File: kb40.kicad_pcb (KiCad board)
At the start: 2 copper layers, 4.8 x 4.8 mm, 73 parts, among them SW1 Choc, SW10 Choc, SW11 Choc, SW12 Choc, SW13 Choc, SW14 Choc, SW15 Choc, SW16 Choc, SW17 Choc, SW18 Choc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

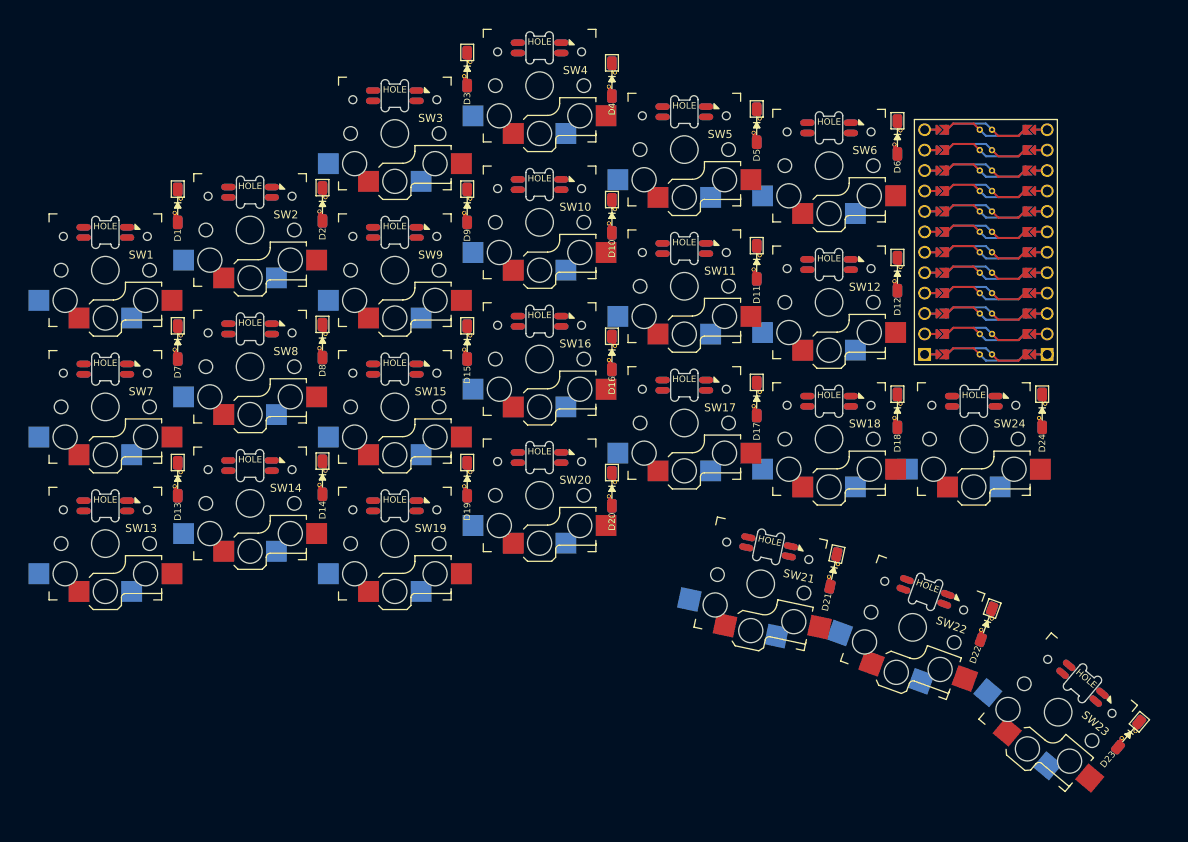
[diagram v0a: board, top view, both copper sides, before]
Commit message: generate test step file
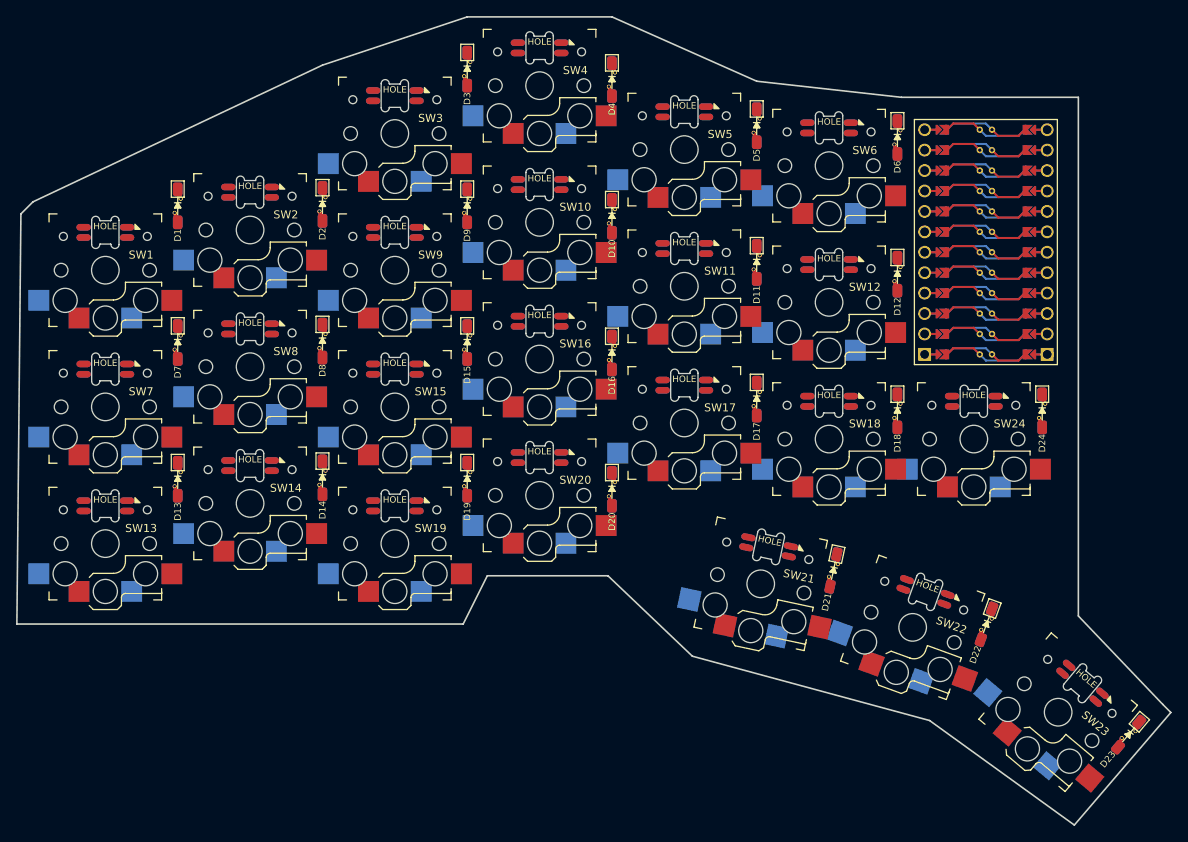
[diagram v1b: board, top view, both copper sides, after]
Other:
- board size 4.8 x 4.8 mm -> 143.5 x 100.5 mm
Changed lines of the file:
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@@
       (net 60 "COL5") (pinfunction "2") (pintype "passive"))
   )
+  (gr_poly
+    (pts
+      (xy 154.5 53)
+      (xy 172.5 55)
+      (xy 194.5 55)
+      (xy 194.5 119.5)
+      (xy 205 130.5)
+      (xy 206 131.5)
+      (xy 194 145.5)
+      (xy 176 132.5)
+      (xy 146.5 124.5)
+      (xy 136 114.5)
+      (xy 121 114.5)
+      (xy 118 120.5)
+      (xy 62.5 120.5)
+      (xy 63 69.5)
+      (xy 64.5 68)
+      (xy 100.5 51)
+      (xy 118.5 45)
+      (xy 136.5 45)
+    ) (layer "Edge.Cuts") (width 0.2) (fill none))
   (group "" (id 1eb147e1-589d-4513-90a6-3c68c18e557f)
     (members

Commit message: initial matrix routing
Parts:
- added J1: TRRS, pro-micro:PJ-320A, F.Cu at (190.5, 110.0)
- added J2: OLED, Connector_PinSocket_2.54mm:PinSocket_1x04_P2.54mm_Vertical, F.Cu at (186.8, 87.8)
- added JP1: SJ, Jumper:SolderJumper-2_P1.3mm_Open_TrianglePad1.0x1.5mm, F.Cu at (178.6, 84.2)
- added JP2: SJ, Jumper:SolderJumper-2_P1.3mm_Open_TrianglePad1.0x1.5mm, F.Cu at (181.4, 84.2)
- added JP3: SJ, Jumper:SolderJumper-2_P1.3mm_Open_TrianglePad1.0x1.5mm, F.Cu at (184.6, 84.2)
- added JP4: SJ, Jumper:SolderJumper-2_P1.3mm_Open_TrianglePad1.0x1.5mm, F.Cu at (187.4, 84.2)
- added JP5: SJ, Jumper:SolderJumper-2_P1.3mm_Open_TrianglePad1.0x1.5mm, B.Cu at (178.6, 84.2)
- added JP6: SJ, Jumper:SolderJumper-2_P1.3mm_Open_TrianglePad1.0x1.5mm, B.Cu at (181.4, 84.2)
- added JP7: SJ, Jumper:SolderJumper-2_P1.3mm_Open_TrianglePad1.0x1.5mm, B.Cu at (184.6, 84.2)
- added JP8: SJ, Jumper:SolderJumper-2_P1.3mm_Open_TrianglePad1.0x1.5mm, B.Cu at (187.4, 84.2)
- moved U1 6.00 mm to (183.0, 67.0), turned to -90 degrees
- moved D1 2.00 mm to (82.5, 70.5)
- moved D13 2.00 mm to (82.5, 104.5)
- moved D14 2.00 mm to (100.5, 104.3)
- moved D2 2.00 mm to (100.5, 70.3)
- moved D7 2.00 mm to (82.5, 87.5)
- moved D8 2.00 mm to (100.5, 87.3)
- moved LED1 2.00 mm to (73.5, 73.8)
- moved LED13 2.00 mm to (73.5, 107.8)
- moved LED14 2.00 mm to (91.5, 102.8)
- moved LED2 2.00 mm to (91.5, 68.8)
- moved LED7 2.00 mm to (73.5, 90.8)
- moved LED8 2.00 mm to (91.5, 85.8)
- moved SW1 2.00 mm to (73.5, 78.5)
- moved SW13 2.00 mm to (73.5, 112.5)
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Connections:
- U1 pad 23: unconnected-(U1-Pad23) -> GND
- U1 pad 3: unconnected-(U1-Pad3) -> GND
- U1 pad 4: unconnected-(U1-Pad4) -> GND
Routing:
- net COL2: track 0.00 -> 201.5 mm, vias 0 -> 6
- net COL3: track 0.00 -> 183.4 mm, vias 0 -> 6
- net COL4: track 0.00 -> 175.5 mm, vias 0 -> 6
- net ROW3: track 0.00 -> 168.8 mm, vias 0 -> 4
- net COL1: track 0.00 -> 166.2 mm, vias 0 -> 5
- net COL0: track 0.00 -> 161.8 mm, vias 0 -> 4
- net ROW1: track 0.00 -> 154.6 mm, vias 0 -> 5
- net ROW0: track 0.00 -> 154.4 mm
- net ROW2: track 0.00 -> 154.0 mm, vias 0 -> 5
- net COL5: track 0.00 -> 122.5 mm, vias 0 -> 4
- net Net-(D9-Pad2): track 0.00 -> 23.5 mm, vias 0 -> 1
- net Net-(D1-Pad2): track 0.00 -> 23.5 mm, vias 0 -> 1
- net Net-(D15-Pad2): track 0.00 -> 23.4 mm, vias 0 -> 1
- net Net-(D7-Pad2): track 0.00 -> 23.4 mm, vias 0 -> 1
- net Net-(D19-Pad2): track 0.00 -> 23.4 mm, vias 0 -> 1
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- added copper zone on B.Cu, net GND
- added copper zone on F.Cu, net GND
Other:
- board size 143.5 x 100.5 mm -> 144.3 x 102.7 mm

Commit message: initial rgb routing
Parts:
- LED1, LED10, LED11, LED12, LED13, LED14, LED15, LED16, LED17, LED18, LED19, LED2, LED20, LED21, LED22, LED23, LED24, LED3, LED4, LED5, LED6, LED7, LED8, LED9: footprint tufourn-components:SK6812Mini-E -> tufourn-components:SK6812-MINI-E
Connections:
- LED1 pad 4: VDD -> VCC
- LED10 pad 4: VDD -> VCC
- LED11 pad 4: VDD -> VCC
- LED12 pad 4: VDD -> VCC
- LED13 pad 4: VDD -> VCC
- LED14 pad 4: VDD -> VCC
- LED15 pad 4: VDD -> VCC
- LED16 pad 4: VDD -> VCC
- LED17 pad 4: VDD -> VCC
- LED18 pad 4: VDD -> VCC
- LED19 pad 4: VDD -> VCC
- LED2 pad 4: VDD -> VCC
- LED20 pad 4: VDD -> VCC
- LED21 pad 4: VDD -> VCC
- LED22 pad 4: VDD -> VCC
- LED23 pad 4: VDD -> VCC
- LED24 pad 4: VDD -> VCC
- LED3 pad 4: VDD -> VCC
- LED4 pad 4: VDD -> VCC
- LED5 pad 4: VDD -> VCC
- LED6 pad 4: VDD -> VCC
- LED7 pad 4: VDD -> VCC
- LED8 pad 4: VDD -> VCC
- LED9 pad 4: VDD -> VCC
- U1 pad 21: unconnected-(U1-Pad21) -> VCC
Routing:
- net VCC: track 0.00 -> 873.1 mm, vias 0 -> 28
- net GND: track 0.00 -> 541.4 mm, vias 0 -> 24
- net Net-(LED6-Pad1): track 0.00 -> 139.9 mm, vias 0 -> 2
- net Net-(LED12-Pad1): track 0.00 -> 126.8 mm, vias 0 -> 2
- net Net-(LED18-Pad1): track 0.00 -> 84.0 mm, vias 0 -> 2
- net Net-(LED23-Pad1): track 0.00 -> 73.3 mm, vias 0 -> 4
- net Net-(LED20-Pad1): track 0.00 -> 37.7 mm, vias 0 -> 2
- net Net-(LED2-Pad1): track 0.00 -> 31.6 mm, vias 0 -> 2
- net Net-(LED8-Pad1): track 0.00 -> 30.8 mm, vias 0 -> 2
- net Net-(LED14-Pad1): track 0.00 -> 29.7 mm, vias 0 -> 2
- net Net-(LED22-Pad1): track 0.00 -> 27.2 mm, vias 0 -> 2
- net Net-(LED21-Pad1): track 0.00 -> 26.2 mm, vias 0 -> 2
- net Net-(LED3-Pad1): track 0.00 -> 26.0 mm, vias 0 -> 2
- net Net-(LED10-Pad1): track 0.00 -> 24.5 mm, vias 0 -> 2
- net Net-(LED4-Pad1): track 0.00 -> 24.0 mm, vias 0 -> 2
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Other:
- board size 144.3 x 102.7 mm -> 144.3 x 103.7 mm

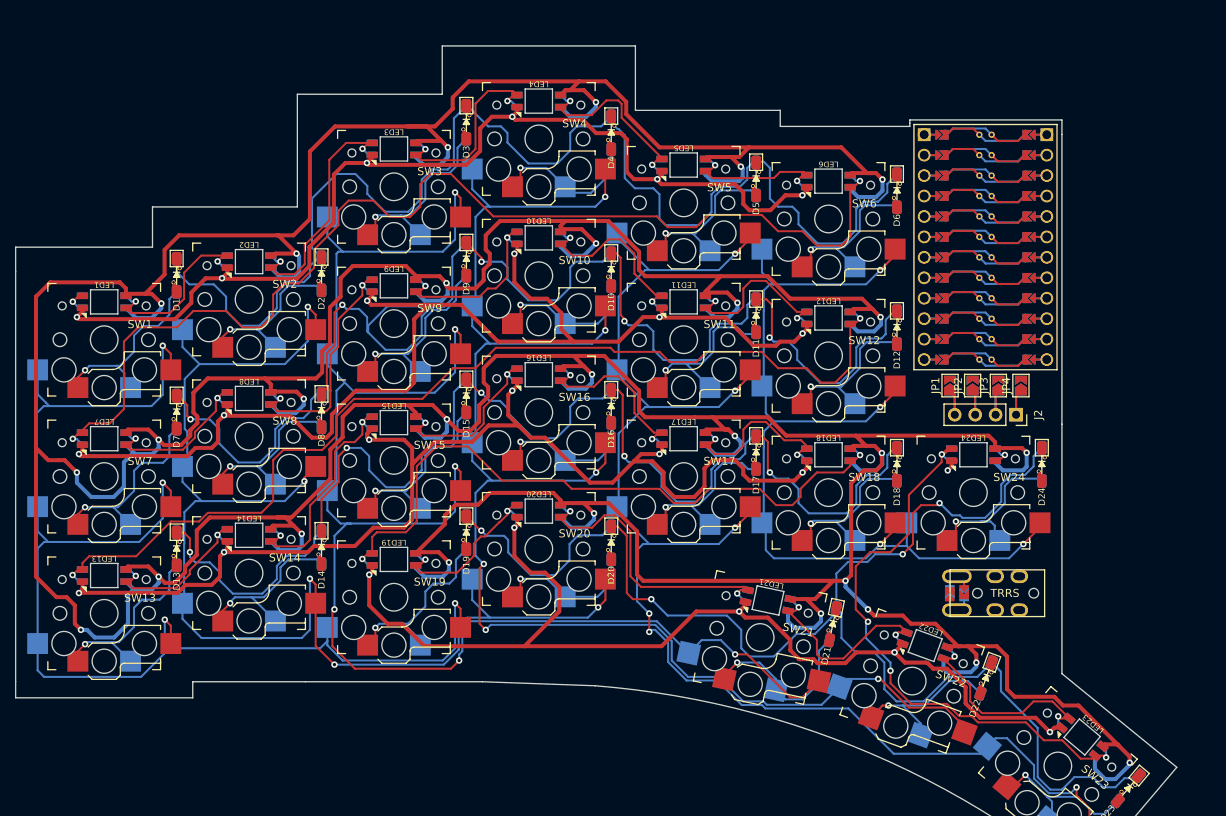
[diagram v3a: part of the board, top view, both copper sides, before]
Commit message: initial completed routing
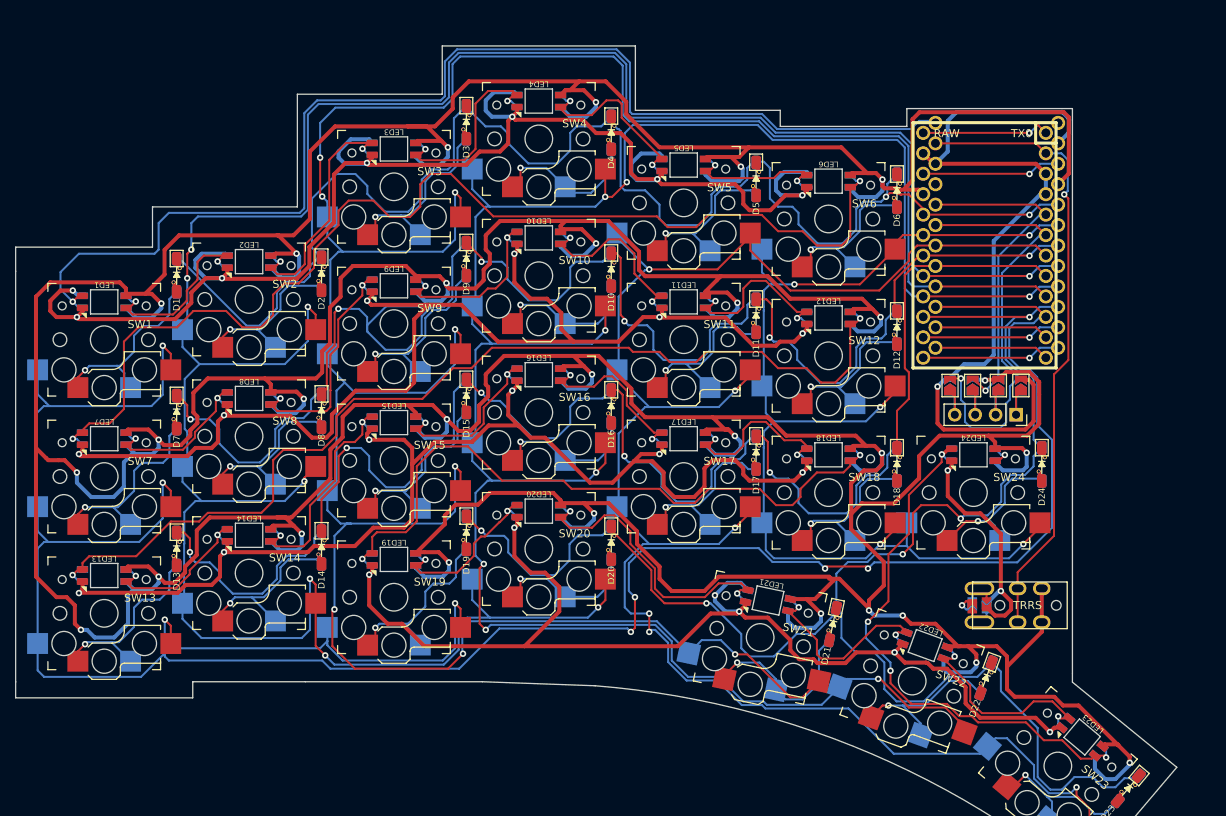
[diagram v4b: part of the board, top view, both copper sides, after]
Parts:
- J1: footprint pro-micro:PJ-320A -> tufourn-components:PJ-320A
- U1: footprint pro-micro:ProMicro -> tufourn-components:ArduinoProMicro-BackSide
- moved J1 3.17 mm to (193.3, 111.5)
- moved U1 2.03 mm to (184.4, 65.5)
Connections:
- J1 pad B: unconnected-(J1-PadB) -> VCC
- J1 pad C: unconnected-(J1-PadC) -> D2
- J1 pad D: unconnected-(J1-PadD) -> GND
- U1 pad 1: unconnected-(U1-Pad1) -> LED
- U1 pad 10: unconnected-(U1-Pad10) -> COL0
- U1 pad 15: unconnected-(U1-Pad15) -> ROW3
- U1 pad 16: unconnected-(U1-Pad16) -> COL3
- U1 pad 17: unconnected-(U1-Pad17) -> COL1
- U1 pad 18: unconnected-(U1-Pad18) -> ROW1
- U1 pad 19: unconnected-(U1-Pad19) -> COL5
- U1 pad 2: unconnected-(U1-Pad2) -> D2
- U1 pad 20: unconnected-(U1-Pad20) -> ROW0
- U1 pad 5: unconnected-(U1-Pad5) -> SDA
- U1 pad 6: unconnected-(U1-Pad6) -> SCL
- U1 pad 7: unconnected-(U1-Pad7) -> COL4
- U1 pad 8: unconnected-(U1-Pad8) -> ROW2
- U1 pad 9: unconnected-(U1-Pad9) -> COL2
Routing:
- net GND: track 541.4 -> 735.1 mm, vias 24 -> 28
- net COL0: track 162.2 -> 336.2 mm, vias 4 -> 8
- net COL1: track 161.6 -> 325.6 mm, vias 5 -> 8
- net LED: track 3.04 -> 161.3 mm
- net COL2: track 202.3 -> 335.9 mm, vias 6 -> 8
- net VCC: track 873.1 -> 963.1 mm, vias 28 -> 29
- net COL3: track 188.3 -> 272.2 mm, vias 6 -> 8
- net D2: track 0.00 -> 77.8 mm, vias 0 -> 1
- net SCL: track 0.00 -> 55.0 mm, vias 0 -> 1
- net COL4: track 177.4 -> 224.2 mm
- net SDA: track 0.00 -> 42.0 mm, vias 0 -> 1
- net ROW2: track 157.3 -> 198.1 mm
- net ROW3: track 171.7 -> 207.2 mm, vias 4 -> 5
- net ROW1: track 173.3 -> 199.0 mm, vias 5 -> 6
- net ROW0: track 158.6 -> 180.8 mm, vias 0 -> 2
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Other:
- outline, holes or cut-outs redrawn

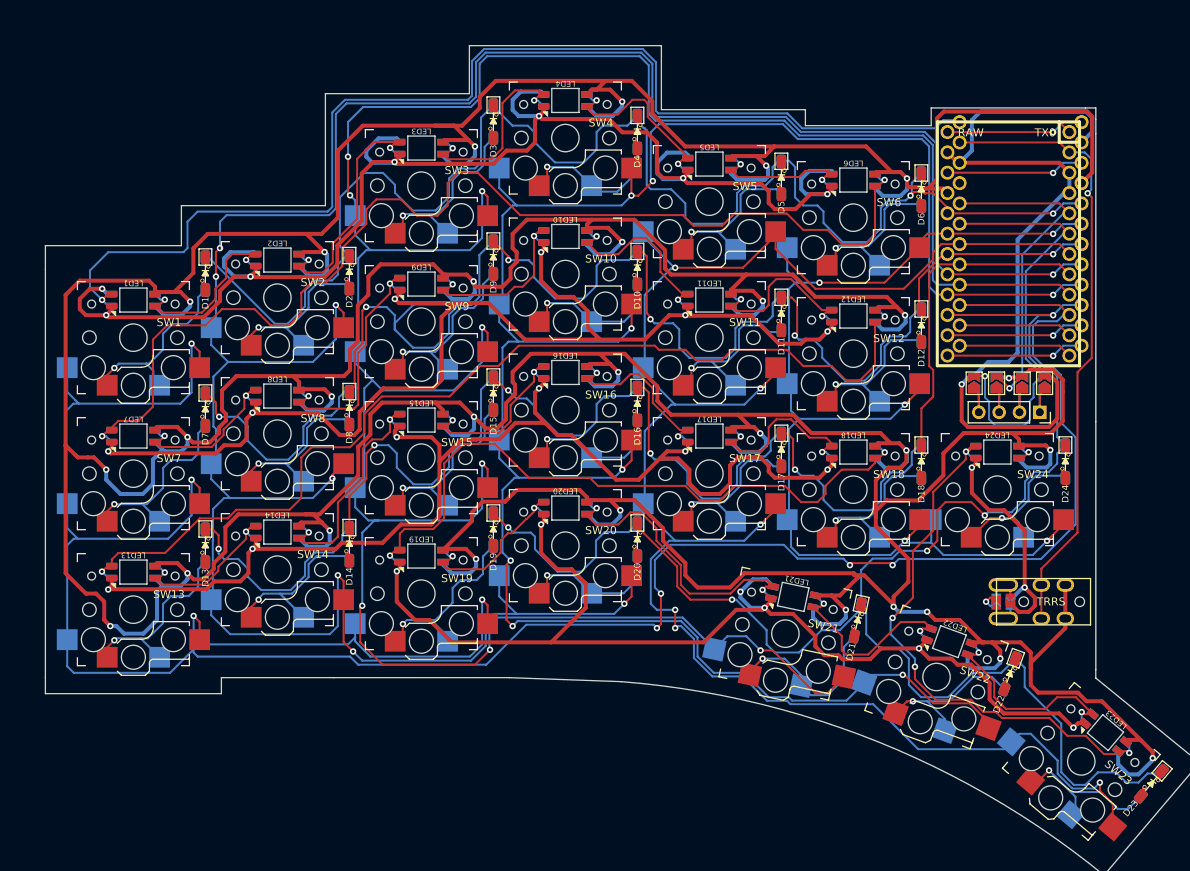
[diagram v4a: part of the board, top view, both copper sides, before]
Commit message: added silkscreen
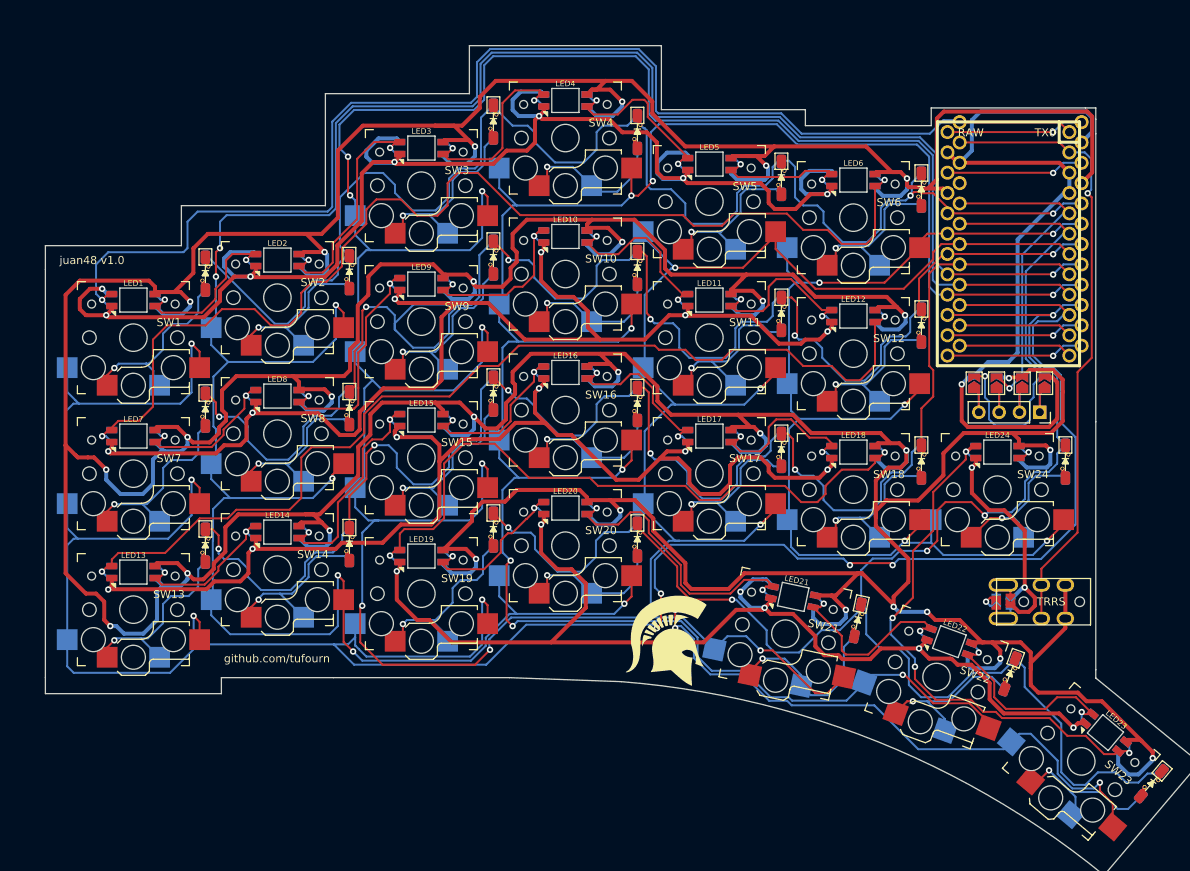
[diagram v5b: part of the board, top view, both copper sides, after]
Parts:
- added G***: LOGO, LOGO, F.Cu at (140.5, 116.1)
- D1, D10, D11, D12, D13, D14, D15, D16, D17, D18, D19, D2, D20, D21, D22, D23, D24, D3, D4, D5, D6, D7, D8, D9: footprint reversible-kicad-footprints:D_SOD-123 -> tufourn-components:D_SOD-123
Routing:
- net COL0: track 336.2 -> 319.0 mm
- net COL1: track 325.6 -> 322.7 mm
- net LED: track 161.3 -> 160.3 mm
- net VCC: track 963.1 -> 963.9 mm
- net COL2: track 335.9 -> 335.1 mm
- net COL3: track 272.2 -> 271.5 mm
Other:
- board text added: "github.com/tufourn"
- board text added: "juan48 v1.0"
